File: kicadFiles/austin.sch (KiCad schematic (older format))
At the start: 479 parts, among them J1 TYPE-C-31-M12_13, J5 Conn_01x06_Male, Q1 AO4406AL, SW1 MXSwitch, SW10 MXSwitch, SW100 MXSwitch, SW101 MXSwitch, SW102 MXSwitch, SW103 MXSwitch, SW104 MXSwitch, SW105 MXSwitch, SW106 MXSwitch, SW107 MXSwitch, SW108 MXSwitch, SW109 MXSwitch, SW11 MXSwitch, SW110 MXSwitch, SW111 MXSwitch, SW112 MXSwitch, SW113 MXSwitch, SW114 MXSwitch, SW12 MXSwitch, SW13 MXSwitch, SW14 MXSwitch, SW15 MXSwitch, SW16 MXSwitch, SW17 MXSwitch, SW18 MXSwitch, SW19 MXSwitch, SW2 MXSwitch, SW20 MXSwitch, SW21 MXSwitch, SW22 MXSwitch, SW23 MXSwitch, SW24 MXSwitch, SW25 MXSwitch, SW26 MXSwitch, SW27 MXSwitch, SW28 MXSwitch, SW29 MXSwitch, SW3 MXSwitch, SW30 MXSwitch, SW31 MXSwitch, SW32 MXSwitch, SW33 MXSwitch, SW34 MXSwitch, SW35 MXSwitch, SW36 MXSwitch, SW37 MXSwitch, SW38 MXSwitch, SW39 MXSwitch, SW4 MXSwitch, SW40 MXSwitch, SW41 MXSwitch, SW42 MXSwitch, SW43 MXSwitch, SW44 MXSwitch, SW45 MXSwitch, SW46 MXSwitch, SW47 MXSwitch, SW48 MXSwitch, SW49 MXSwitch, SW5 MXSwitch, SW50 MXSwitch, SW51 MXSwitch, SW52 MXSwitch, SW53 MXSwitch, SW54 MXSwitch, SW55 MXSwitch, SW56 MXSwitch, SW57 MXSwitch, SW58 ANSI LShift, SW59 MXSwitch, SW6 MXSwitch, SW60 MXSwitch, SW61 MXSwitch, SW62 MXSwitch, SW63 MXSwitch, SW64 MXSwitch, SW65 MXSwitch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

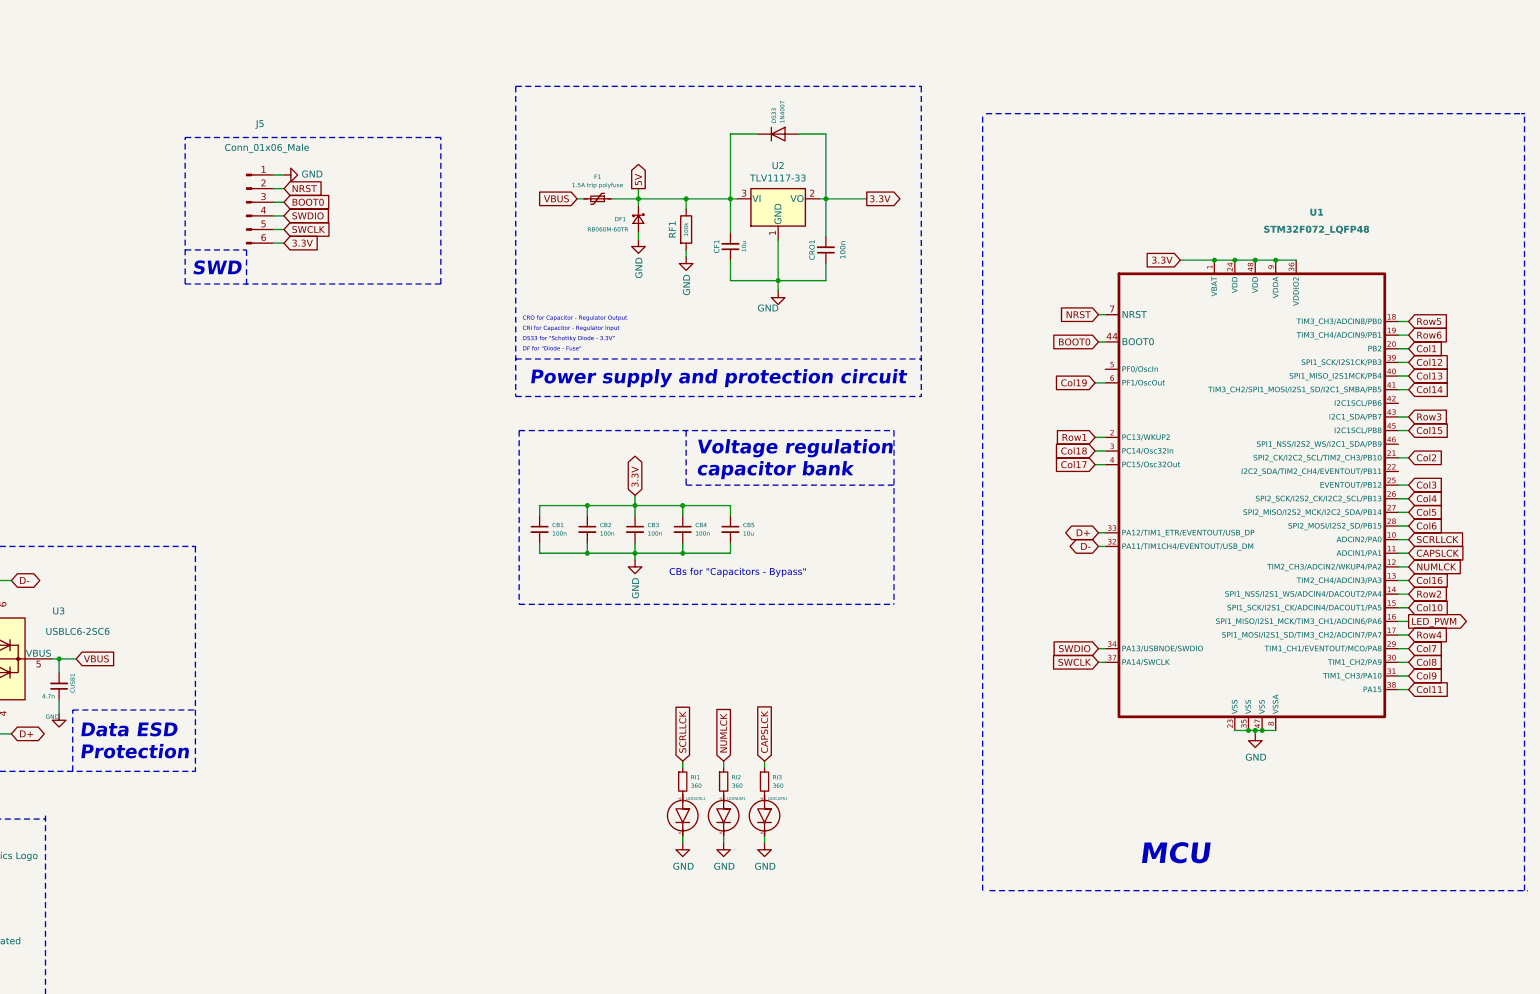
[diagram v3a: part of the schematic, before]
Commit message: Change SWD JTAG pins
- The SWD JTAG headers were placed in the wrong order. This has been fixed
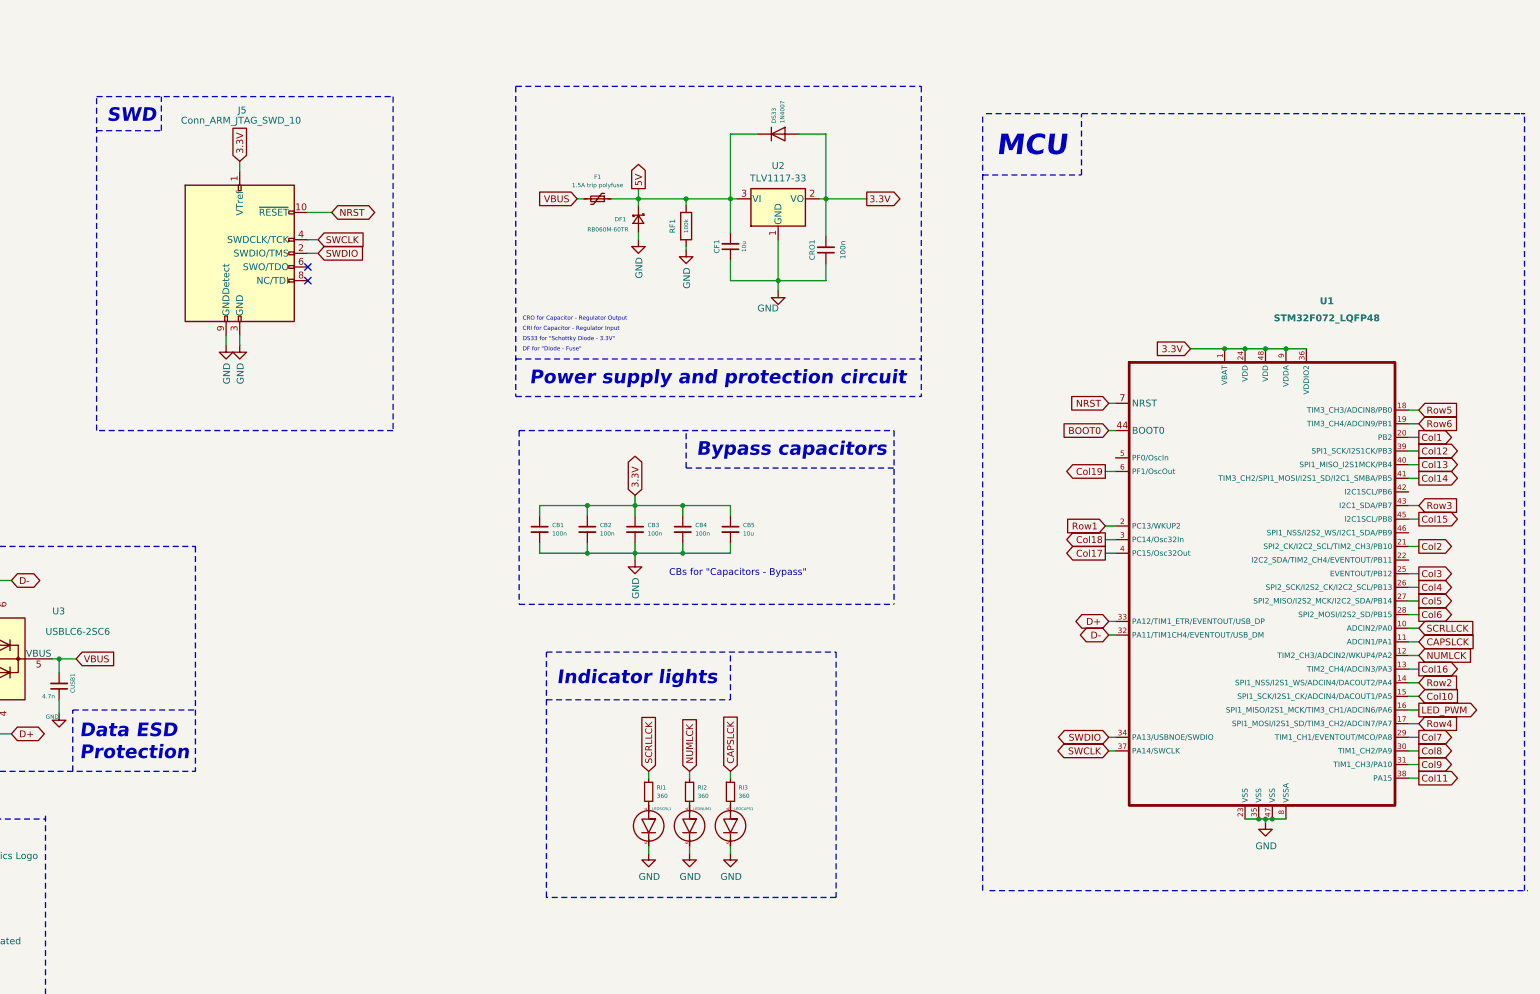
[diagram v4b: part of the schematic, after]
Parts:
- removed J5: Conn_01x06_Male, acheronConnectors:HEADER_6PIN_HORIZONTAL, symbol Connector:Conn_01x06_Male
- added J5: Conn_ARM_JTAG_SWD_10, Connector_PinHeader_2.54mm:PinHeader_2x05_P2.54mm_Vertical, symbol Connector:Conn_ARM_JTAG_SWD_10
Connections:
- net 3.3V: now also J5.1 (VTref)
- net GND: now also J5.3 (GND), J5.5 (GND), J5.9 (GNDDetect)
- net NRST: now also J5.10 (~RESET~)
- net SWCLK: now also J5.4 (SWDCLK/TCK)
- net SWDIO: now also J5.2 (SWDIO/TMS)
- no-connect marks 2 -> 4
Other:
- note added: "Bypass capacitors"
- note added: "Indicator lights"
- note removed: "Voltage regulation\ncapacitor bank\n"
- moved on the sheet: LEDCAPS1, LEDNUM1, LEDSCRL1, RF1, RI1, RI2, RI3, U1

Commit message: Implement schematic changes to PCB
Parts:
- added LED59, LED96: LED, acheronComponents:LED_THT_2.54mm, symbol austin-rescue:LED-acheronSymbols
- added RL35: 360, acheronComponents:R_SMD_1026, symbol Device:R_Small
- gave numbers to parts that had none: 1
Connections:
- net 5V: now also RL35.1
- net Col1: now also U1.21 (SPI2_CK/I2C2_SCL/TIM2_CH3/PB10); no longer U1.20 (PB2)
- net Col2: now also U1.22 (I2C2_SDA/TIM2_CH4/EVENTOUT/PB11); no longer U1.21 (SPI2_CK/I2C2_SCL/TIM2_CH3/PB10)
- net LEDK: now also LED59.K, LED96.K
- net Row3: now also U1.17 (SPI1_MOSI/I2S1_SD/TIM3_CH2/ADCIN7/PA7); no longer U1.43 (I2C1_SDA/PB7)
- net Row4: now also U1.18 (TIM3_CH3/ADCIN8/PB0); no longer U1.17 (SPI1_MOSI/I2S1_SD/TIM3_CH2/ADCIN7/PA7)
- net Row5: now also U1.19 (TIM3_CH4/ADCIN9/PB1); no longer U1.18 (TIM3_CH3/ADCIN8/PB0)
- net Row6: now also U1.20 (PB2); no longer U1.19 (TIM3_CH4/ADCIN9/PB1)
- net at LED79.A, RL79.2: now also LED59.A
- new net: LED96.A, RL35.2
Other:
- moved on the sheet: J5, L1, L2, L3, L4, L5, L6, LED112

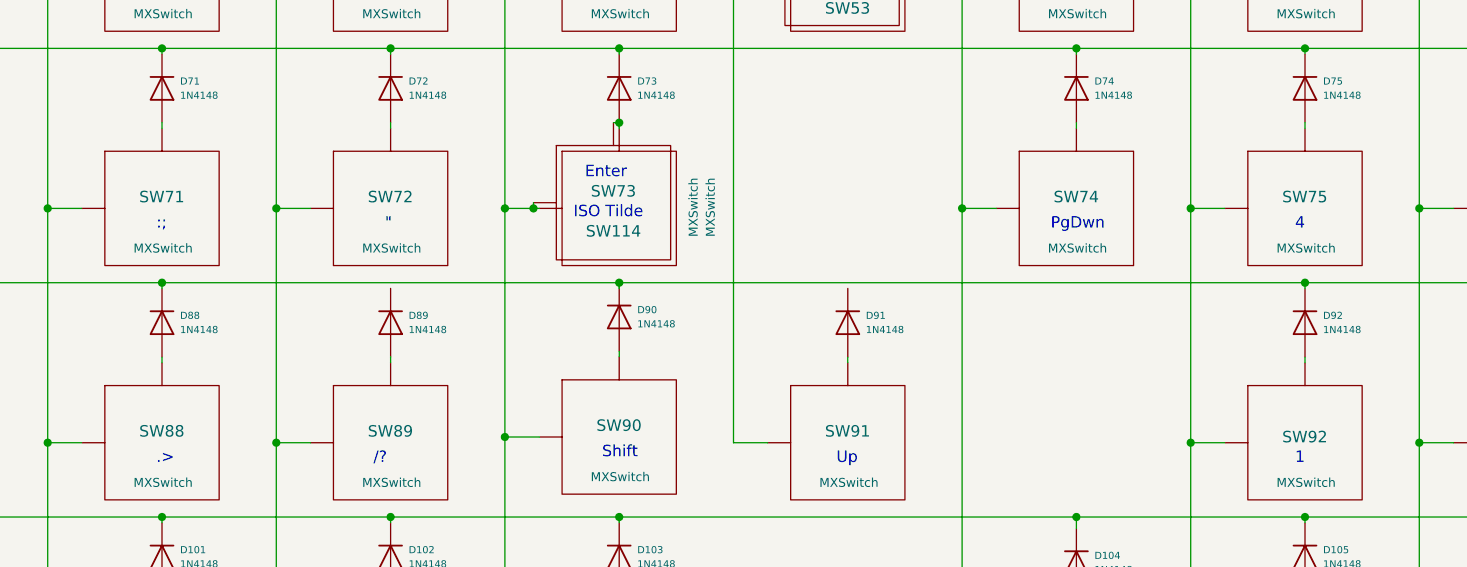
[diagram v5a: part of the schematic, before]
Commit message: Run DRC and solve issues
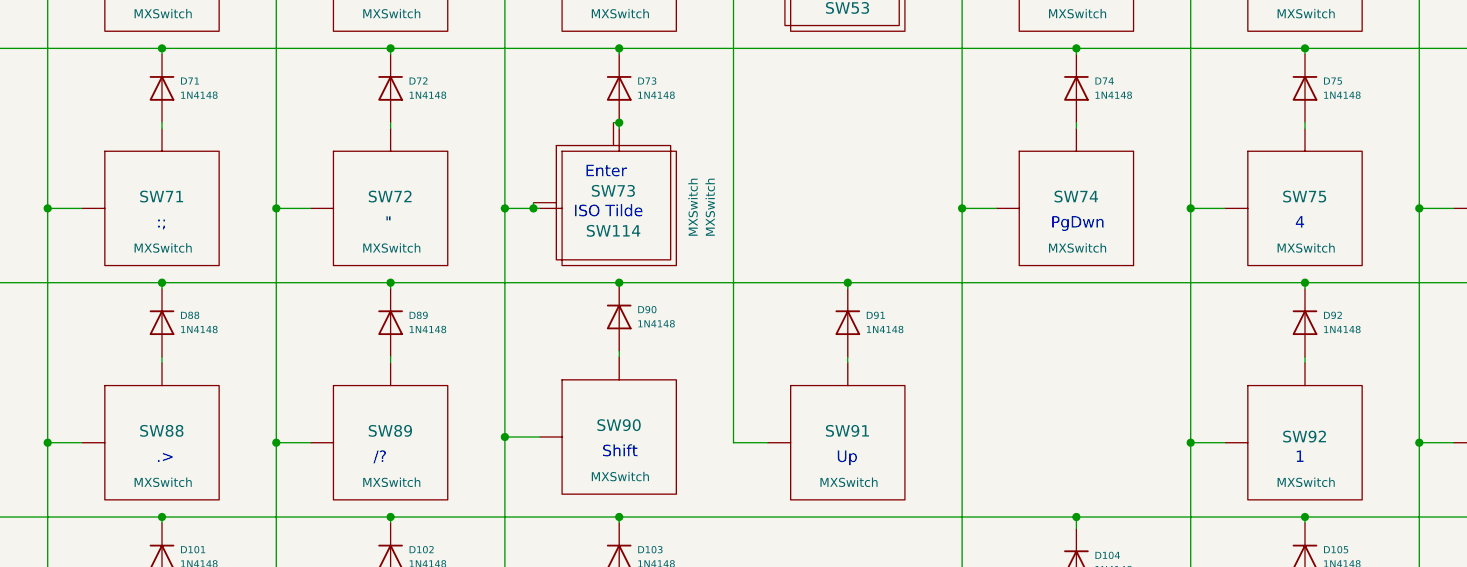
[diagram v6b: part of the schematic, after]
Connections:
- net Row5: now also D89.1 (K), D91.1 (K)
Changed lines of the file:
@@
 	15600 5850 15600 5825
 Wire Wire Line
-	14600 5525 14600 5500
-Wire Wire Line
 	13250 6200 13100 6200
 Wire Wire Line
@@
 Connection ~ 14600 5500
 Wire Wire Line
-	14600 5500 17600 5500
+	14600 5500 15600 5500
 Wire Wire Line
 	1750 6525 2600 6525
@@
 	3100 5175 3100 6200
 Wire Wire Line
-	12600 5500 14600 5500
+	12600 5500 13600 5500
 $Comp
 L Device:D D34
@@
 Wire Wire Line
 	5300 12675 5550 12675
+Wire Wire Line
+	13600 5500 13600 5525
+Connection ~ 13600 5500
+Wire Wire Line
+	13600 5500 14600 5500
+Wire Wire Line
+	15600 5525 15600 5500
+Connection ~ 15600 5500
+Wire Wire Line
+	15600 5500 17600 5500
 $EndSCHEMATC
